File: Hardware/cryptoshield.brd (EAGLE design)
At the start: 59.7 x 53.3 mm, 49 parts, among them J1 AVR_SPI_PRG_6PTH, Q1 BSS138, Q2 BSS138, Q3 BSS138, Q4 MOSFET-PCH, U1 33mhz

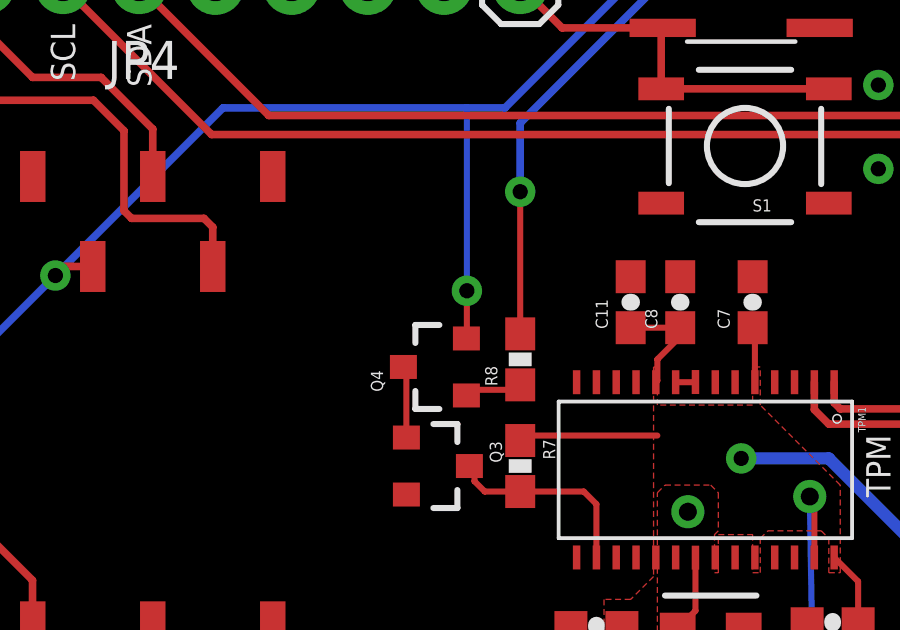
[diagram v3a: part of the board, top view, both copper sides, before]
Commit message: made changed to isolate Reset from 5V
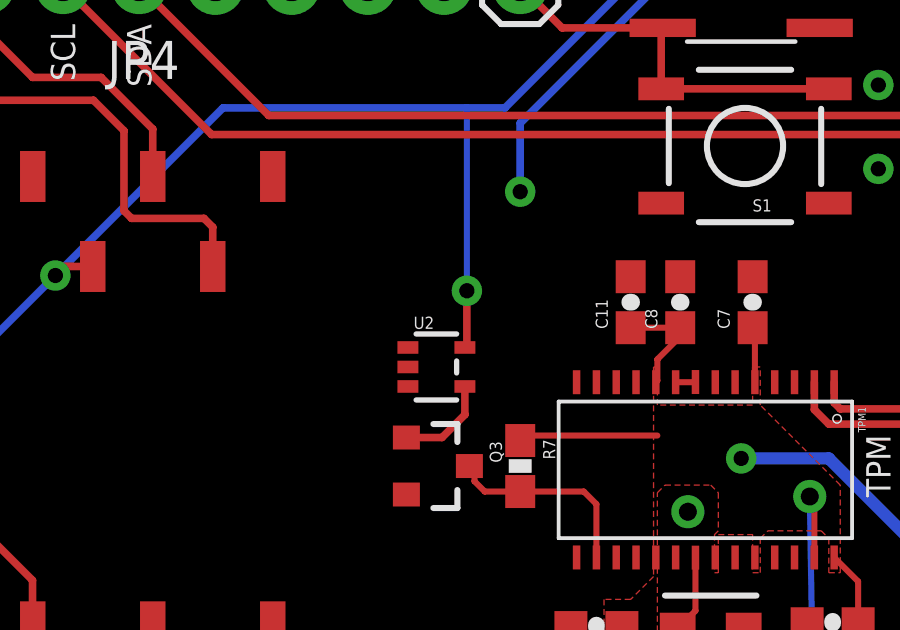
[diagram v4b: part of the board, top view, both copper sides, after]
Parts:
- removed Q4: MOSFET-PCH, SparkFun-DiscreteSemi:SOT23-3
- removed R8: 10K, SparkFun:0603-RES
- added U2: 74LVC1G04, SparkFun-DigitalIC:SOT353
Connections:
- removed net N$21: Q4.1, R8.1
- net !RESET: now also U2.2; no longer R8.2
- net GND: now also U2.3
- net N$20: now also U2.4; no longer Q4.3
- net VCCIO: now also U2.5; no longer Q4.2
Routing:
- net !RESET: track 32.8 -> 28.1 mm
- net N$21: track 2.13 -> 0.00 mm
- net N$20: track 2.39 -> 3.21 mm
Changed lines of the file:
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@@
 <layer number="56" name="wert" color="7" fill="1" visible="no" active="no"/>
 <layer number="57" name="tCAD" color="7" fill="1" visible="no" active="no"/>
+<layer number="90" name="Modules" color="5" fill="1" visible="yes" active="yes"/>
 <layer number="91" name="Nets" color="2" fill="1" visible="no" active="no"/>
 <layer number="92" name="Busses" color="1" fill="1" visible="no" active="no"/>
@@
 <layer number="251" name="SMDround" color="12" fill="11" visible="no" active="no"/>
 <layer number="254" name="cooling" color="7" fill="1" visible="yes" active="yes"/>
+<layer number="255" name="routoute" color="7" fill="1" visible="yes" active="yes"/>
 </layers>
 <board>
@@
 </element>
 <element name="R7" library="SparkFun" package="0603-RES" value="10K" x="34.29" y="18.288" rot="R270"/>
-<element name="Q4" library="SparkFun-DiscreteSemi" package="SOT23-3" value="MOSFET-PCH" x="31.496" y="21.59" rot="R90">
-<attribute name="PROD_ID" value="TRANS-08285" x="31.496" y="21.59" size="1.778" layer="27" rot="R90" display="off"/>
-</element>
-<element name="R8" library="SparkFun" package="0603-RES" value="10K" x="34.29" y="21.844" rot="R90"/>
+<element name="U2" library="SparkFun-DigitalIC" package="SOT353" value="74LVC1G04" x="31.496" y="21.59" rot="R270">
+<attribute name="PROD_ID" value="10843" x="31.496" y="21.59" size="1.778" layer="27" rot="R270" display="off"/>
+</element>
 </elements>
 <signals>
@@
 <via x="47.498" y="28.194" extent="1-16" drill="0.508"/>
 <contactref element="Q3" pad="2"/>
+<contactref element="U2" pad="3"/>
 </signal>
 <signal name="RST">
@@
 <wire x1="24.384" y1="30.226" x2="18.796" y2="24.638" width="0.254" layer="16"/>
 <wire x1="38.1" y1="39.878" x2="38.1" y2="50.8" width="0.254" layer="1"/>
-<contactref element="Q4" pad="2"/>
-<wire x1="32.496" y1="22.54" x2="32.512" y2="22.556" width="0.2032" layer="1"/>
-<wire x1="32.512" y1="22.556" x2="32.512" y2="24.13" width="0.2032" layer="1"/>
 <via x="32.512" y="24.13" extent="1-16" drill="0.508"/>
 <wire x1="32.512" y1="24.13" x2="32.512" y2="30.226" width="0.2032" layer="16"/>
+<contactref element="U2" pad="5"/>
+<wire x1="32.446" y1="22.24" x2="32.512" y2="22.306" width="0.254" layer="1"/>
+<wire x1="32.512" y1="22.306" x2="32.512" y2="24.13" width="0.254" layer="1"/>
 </signal>
 <signal name="N$18">
@@
 <wire x1="33.108" y1="17.438" x2="34.29" y2="17.438" width="0.2032" layer="1"/>
 </signal>
-<signal name="N$20">
-<contactref element="Q3" pad="1"/>
-<contactref element="Q4" pad="3"/>
-<wire x1="30.396" y1="21.59" x2="30.496" y2="21.49" width="0.2032" layer="1"/>
-<wire x1="30.496" y1="21.49" x2="30.496" y2="19.238" width="0.2032" layer="1"/>
-</signal>
-<signal name="N$21">
-<contactref element="Q4" pad="1"/>
-<contactref element="R8" pad="1"/>
-<wire x1="32.496" y1="20.64" x2="32.684" y2="20.828" width="0.2032" layer="1"/>
-<wire x1="32.684" y1="20.828" x2="34.29" y2="20.828" width="0.2032" layer="1"/>
-<wire x1="34.29" y1="20.828" x2="34.29" y2="20.994" width="0.2032" layer="1"/>
-<wire x1="34.29" y1="21.082" x2="34.29" y2="20.994" width="0.2032" layer="1"/>
-</signal>
 <signal name="!RESET">
-<contactref element="R8" pad="2"/>
 <contactref element="U$1" pad="RES"/>
 <wire x1="35.56" y1="50.8" x2="36.576" y2="49.784" width="0.254" layer="1"/>
@@
 <wire x1="34.29" y1="29.718" x2="34.29" y2="27.432" width="0.254" layer="16"/>
 <via x="34.29" y="27.432" extent="1-16" drill="0.508"/>
-<wire x1="34.29" y1="22.694" x2="34.29" y2="27.432" width="0.2032" layer="1"/>
+<contactref element="U2" pad="2"/>
+<wire x1="30.546" y1="21.59" x2="34.29" y2="27.432" width="0" layer="19" extent="1-16"/>
+</signal>
+<signal name="N$20">
+<contactref element="Q3" pad="1"/>
+<contactref element="U2" pad="4"/>
+<wire x1="32.446" y1="20.94" x2="32.446" y2="20" width="0.254" layer="1"/>
+<wire x1="32.446" y1="20" x2="31.684" y2="19.238" width="0.254" layer="1"/>
+<wire x1="31.684" y1="19.238" x2="30.496" y2="19.238" width="0.254" layer="1"/>
 </signal>
 </signals>

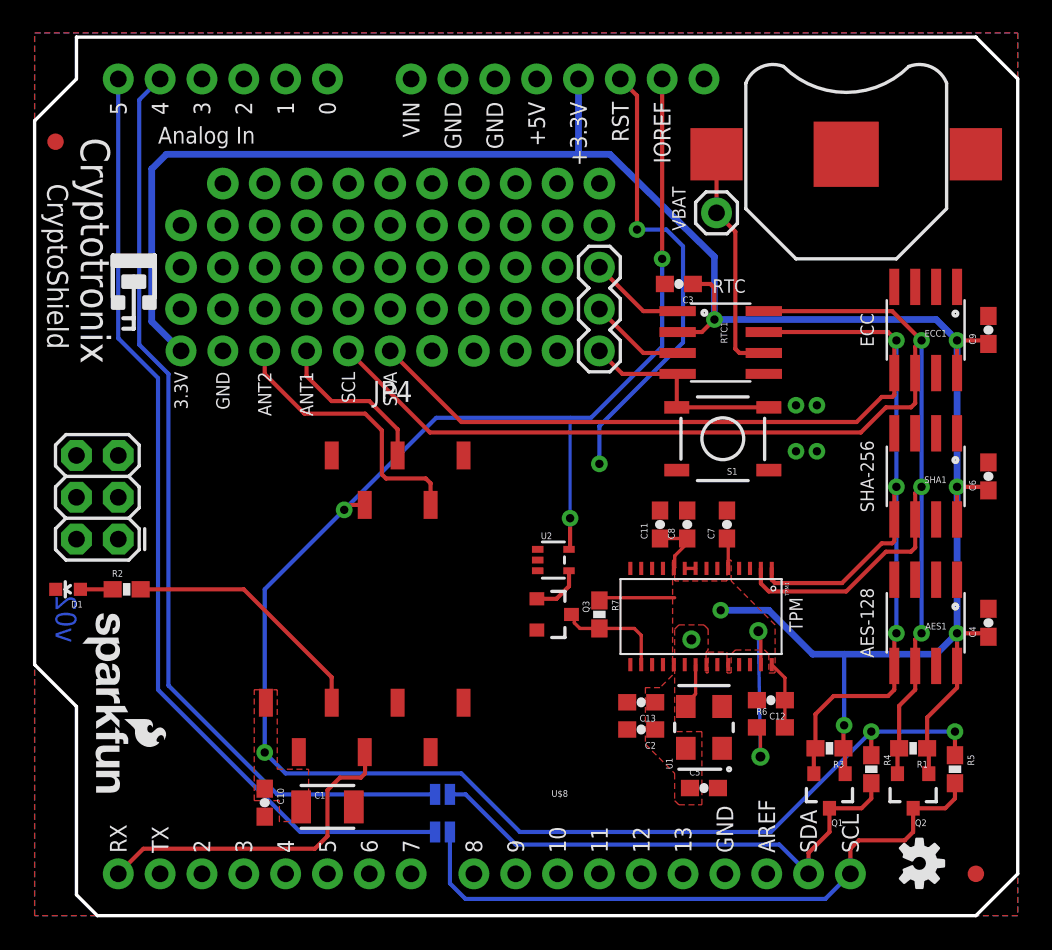
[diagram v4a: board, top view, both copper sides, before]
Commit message: modified layout to meet checklist compliance
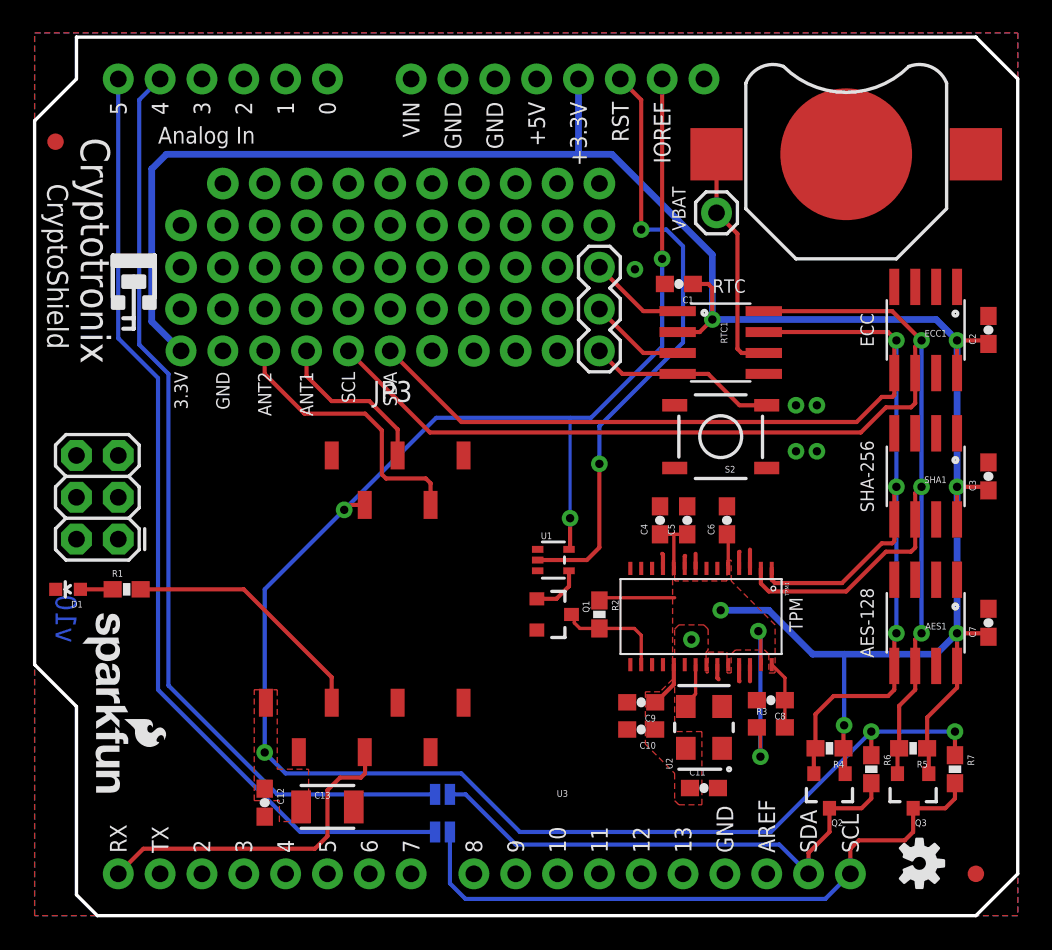
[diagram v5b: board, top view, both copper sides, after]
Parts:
- removed FRAME1: FRAME-LEDGER, SparkFun-Aesthetics:CREATIVE_COMMONS
- removed S1: (no value), SparkFun-Electromechanical:TACTILE-SWITCH-SMD
- added FRAME2: (no value), SparkFun-Aesthetics:CREATIVE_COMMONS
- added S2: Reset, SparkFun-Electromechanical:TACTILE-SWITCH-SMD
- AES1, ECC1, RTC1: device cryptotronix:SOIC8 -> SparkFun-DigitalIC:SOIC8
- C1: value 10uF -> 0.1uF; device SparkFun-Capacitors:1210 -> SparkFun-Capacitors:0603-CAP
- C10, C4: value 0.1uF -> .1uf
- C12, C7: value 2200pf -> 0.1uF
- C13: value 2200pf -> 10uF; device SparkFun-Capacitors:0603-CAP -> SparkFun-Capacitors:1210
- C2: value .1uf -> 0.1uF
- C5: value .1uf -> 2200pf
- C6, C9: value 0.1uF -> 2200pf
- R1: value 10K -> 1k; device SparkFun:0603-RES -> SparkFun-Resistors:0603-RES
- R2: value 1k -> 10K
- R3: value 10K -> 4.7K; device SparkFun:0603-RES -> SparkFun-Resistors:0603
- R4, R5, R7: device SparkFun:0603-RES -> SparkFun-Resistors:0603-RES
- R6: value 4.7K -> 10K; device SparkFun-Resistors:0603 -> SparkFun-Resistors:0603-RES
- SHA1: value ATSHA204 -> ATSHA204_SOIC8; device cryptotronix:SOIC8 -> SparkFun-DigitalIC:SOIC8
- TPM1: device cryptotronix:TSSOP28 -> SparkFun-DigitalIC:TSSOP28
- U1: value 33mhz -> 74LVC1G04; device cryptotronix:CRYSTAL-OSC-SMD-5X3.2 -> SparkFun-DigitalIC:SOT353
- U2: value 74LVC1G04 -> 33mhz; device SparkFun-DigitalIC:SOT353 -> SparkFun-FreqCtrl:CRYSTAL-OSC-SMD-5X3.2
- moved R1 48.7 mm to (5.59, 19.8), turned to 0 degrees
- moved C1 38.3 mm to (39.1, 38.4), turned to 180 degrees
- moved C2 32.1 mm to (57.9, 35.6), turned to 90 degrees
- moved C12 31.4 mm to (14.0, 6.86), turned to 270 degrees
- moved C9 30.9 mm to (36.8, 13.0), turned to 180 degrees
- moved R2 28.7 mm to (34.3, 18.3), turned to 270 degrees
- moved Q3 24.3 mm to (53.3, 7.62), turned to 180 degrees
- moved R7 23.5 mm to (55.9, 8.89)
- moved C10 23.3 mm to (36.8, 11.3), turned to 180 degrees
- moved C3 22.1 mm to (57.9, 26.7), turned to 90 degrees
- moved C4 20.9 mm to (38.0, 24.0)
- moved C13 20.1 mm to (17.8, 6.60), turned to 0 degrees
- moved Q1 19.9 mm to (31.5, 18.3), turned to 270 degrees
- moved C7 17.0 mm to (57.9, 17.8)
- moved C5 16.3 mm to (39.6, 24.0), turned to 90 degrees
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- renumbered JP4 to JP3, SJ1 to SJ101, SJ2 to SJ100, U$1 to U4, U$4 to U$2, U$5 to U$101, U$6 to U$100, U$8 to U3
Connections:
- removed net AUTH0: AES1.2
- net !RESET: now also U1.2; no longer U2.2
- net 3.3V: now also C1.1, C10.1, Q3.1, R2.1, R3.2, R4.1, R5.1, U2.4; no longer C12.1, C13.1, Q1.1, R1.1, R3.1, R6.2, R7.1, U1.4
- net GND: now also Q1.2, S2.1, U1.3, U2.2; no longer Q3.2, S1.1, S1.2, U1.2, U2.3
- net N$1: now also R1.2; no longer R2.2
- net N$12: now also R1.1; no longer R2.1
- net N$18: now also Q1.3, R2.2; no longer Q3.3, R7.2
- net N$19: now also R3.1; no longer R6.1
- net N$20: now also Q1.1, U1.4; no longer Q3.1, U2.4
- net PP: now also S2.3; no longer S1.3, S1.4
- net SCL: now also Q3.2, R5.2; no longer Q2.2, R1.2
- net SCL_IN: now also Q3.3, R7.2; no longer Q2.3, R5.2
- net SDA: now also Q2.2, R4.2; no longer Q1.2, R3.2
- net SDA_IN: now also Q2.3, R6.2; no longer Q1.3, R4.2
- net TPM_CLK: now also U2.3; no longer U1.3
- net VCCIO: now also C12.1, C13.1, R6.1, R7.1, U1.5; no longer C1.1, C10.1, R4.1, R5.1, U2.5
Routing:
- net !RESET: track 28.1 -> 37.1 mm
- net GND: track 0.66 -> 7.71 mm, vias 5 -> 6
- net 3.3V: track 153.6 -> 156.4 mm
- net PP: track 13.0 -> 11.7 mm
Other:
- board text added: "v10"
- board text removed: "Josh Datko / Casey Kuhns"
- board text removed: "v02"

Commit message: fixed all github issues
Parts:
- removed U$2: (no value), SparkFun-Aesthetics:SFE_LOGO_NAME_FLAME_.1
- added LOGO3: SFE_LOGO_NAME_FLAME.1_INCH, SparkFun-Aesthetics:SFE_LOGO_NAME_FLAME_.1
- LOGO2: value (none) -> OSHW-LOGOS
- flipped LOGO2 to the top, turned to 270 degrees
- renumbered AES1 to U5, D1 to STAT, ECC1 to U9, RTC1 to U7, SHA1 to U8, SJ100 to A5, SJ101 to A4, TPM1 to U6, U$100 to LOGO2
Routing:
- net GND: vias 6 -> 5
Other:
- board text added: "32kHz"
- board text added: "PP"
- board text added: "RFID ID-12"
- board text added: "SQW"
- board text added: "STAT"
- board text added: "v02"
- board text removed: "v10"
